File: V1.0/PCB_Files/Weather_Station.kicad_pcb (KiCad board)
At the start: 2 copper layers, 45 parts, among them J1 N091-2832TSWFG02-H14, J2 USB_B_Micro, J3 Conn_01x04_Pin, J4 Conn_01x04_Pin, J5 Conn_01x06_Pin, U1 STM32F103C8T6, U2 HDC1080DMBR, U3 AMS1117-3.3, U5 SRV05-4, Y1 X322516MLB4SI

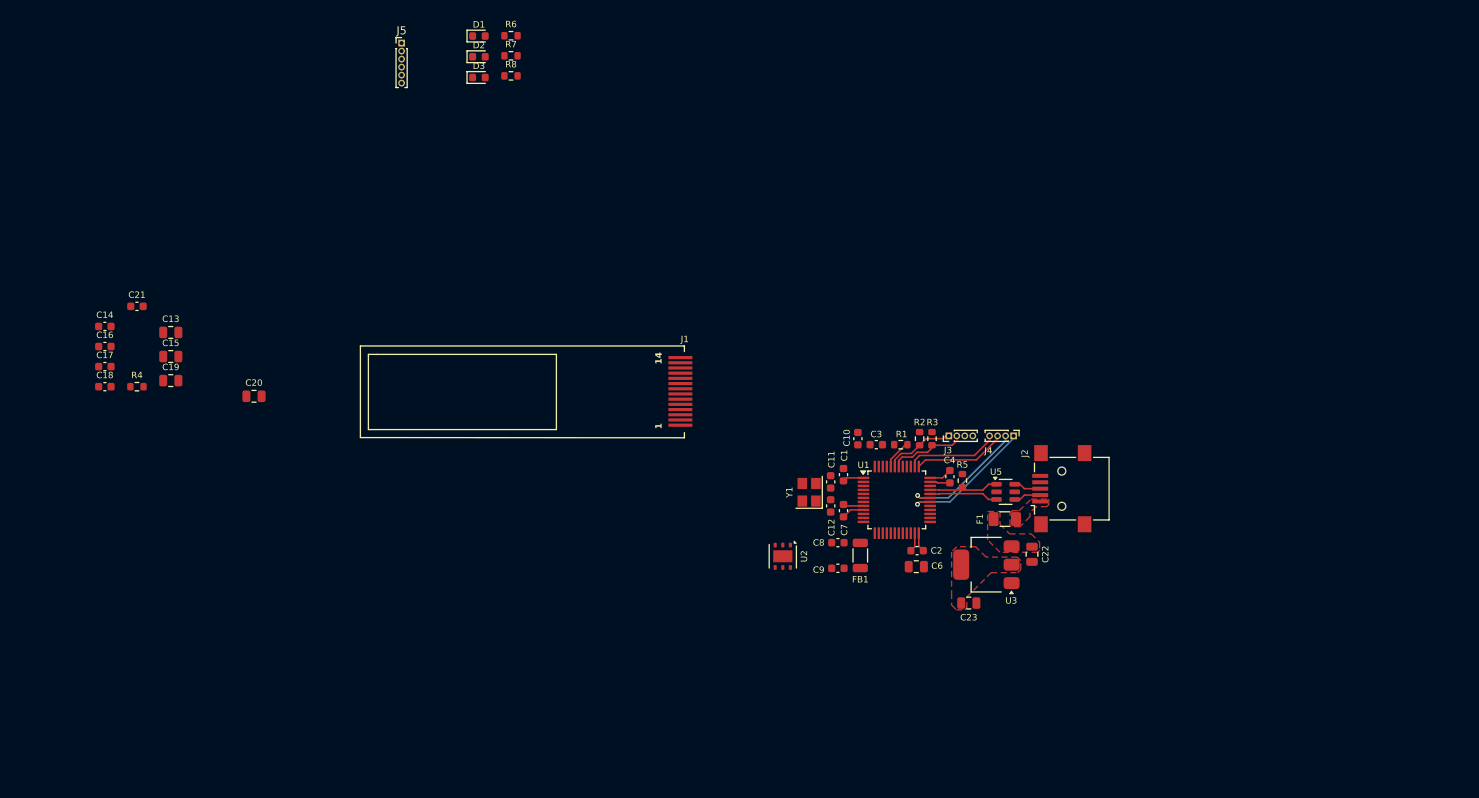
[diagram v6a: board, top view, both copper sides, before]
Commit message: Decided to not go with the display. Added Step file for display.
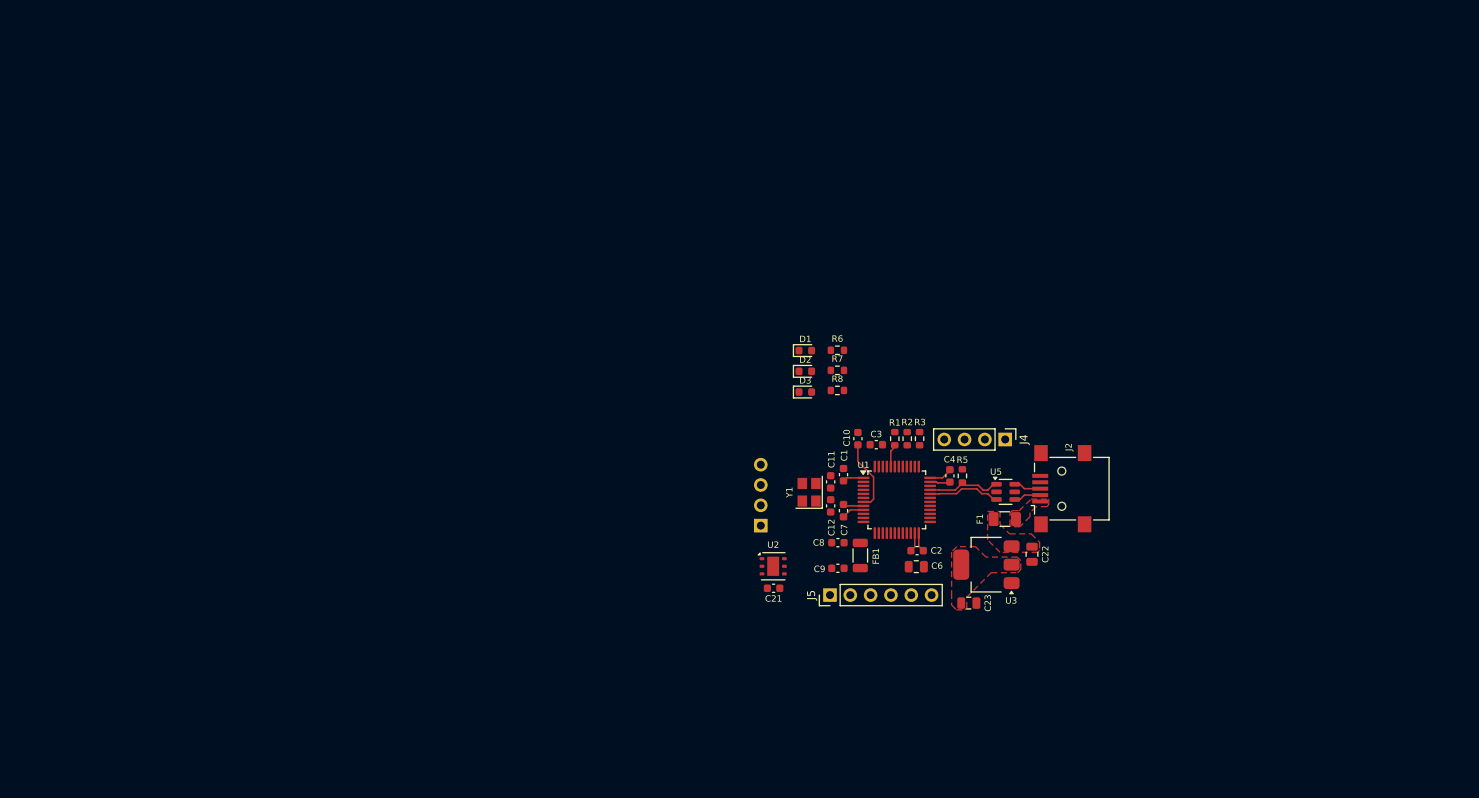
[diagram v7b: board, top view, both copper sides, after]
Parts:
- removed C13: 4u7/16V, Capacitor_SMD:C_0805_2012Metric
- removed C14: 100n/16V, Capacitor_SMD:C_0603_1608Metric
- removed C15: 2u2/16V, Capacitor_SMD:C_0805_2012Metric
- removed C16, C17: 1u/16V, Capacitor_SMD:C_0603_1608Metric
- removed C18: 100n/10V, Capacitor_SMD:C_0603_1608Metric
- removed C19, C20: 4u7/10V, Capacitor_SMD:C_0805_2012Metric
- removed R4: 910k, Resistor_SMD:R_0603_1608Metric
- J1: value N091-2832TSWFG02-H14 -> Conn_01x04_Socket; footprint Private_Connector_Display:OLED_SMD_128x32 -> Capacitor_SMD:C_0402_1005Metric; moved to B.Cu
- J3: footprint Connector_PinHeader_1.00mm:PinHeader_1x04_P1.00mm_Vertical -> Connector_PinHeader_2.54mm:PinHeader_1x04_P2.54mm_Vertical; moved to B.Cu
- J4: footprint Connector_PinHeader_1.00mm:PinHeader_1x04_P1.00mm_Vertical -> Connector_PinHeader_2.54mm:PinHeader_1x04_P2.54mm_Vertical
- J5: footprint Connector_PinHeader_1.00mm:PinHeader_1x06_P1.00mm_Vertical -> Connector_PinHeader_2.54mm:PinHeader_1x06_P2.54mm_Vertical
- moved J5 87.3 mm to (156.9, 94.8), turned to 90 degrees
- moved C21 87.0 mm to (149.9, 94.0)
- moved D3 56.7 mm to (153.9, 69.4)
- moved D1 56.7 mm to (153.9, 64.2)
- moved D2 56.7 mm to (153.9, 66.8)
- moved R6 56.7 mm to (157.9, 64.2)
- moved R8 56.7 mm to (157.9, 69.2)
- moved R7 56.7 mm to (157.9, 66.7)
- moved J3 26.0 mm to (148.3, 86.1), turned to 0 degrees
- moved J1 25.1 mm to (146.8, 88.7)
- moved U2 1.73 mm to (149.8, 91.2), turned to 0 degrees
- moved R2 1.55 mm to (166.6, 75.2)
- moved R3 1.55 mm to (168.2, 75.2)
- moved J4 1.14 mm to (178.8, 75.3)
- moved R1 1.06 mm to (165.1, 75.2), turned to -90 degrees
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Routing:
- net /USART1_TX: track 17.4 -> 0.00 mm, vias 1 -> 0
- net /USART1_RX: track 16.4 -> 0.00 mm, vias 1 -> 0
- net /SWDIO: track 11.7 -> 0.00 mm
- net /SWCLK: track 11.6 -> 0.00 mm
- net /I2C1_SCL: track 9.83 -> 0.00 mm
- net /NRST: track 0.00 -> 9.00 mm
- net /I2C1_SDA: track 8.83 -> 0.00 mm
- net /BOOT0: track 3.74 -> 2.87 mm

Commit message: Should be final component placement.
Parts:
- moved R6 10.2 mm to (153.0, 73.2)
- moved D1 9.80 mm to (149.9, 73.2)
- moved R7 9.49 mm to (153.0, 74.8)
- moved D2 8.94 mm to (149.9, 74.8)
- moved R8 8.72 mm to (153.0, 76.5)
- moved D3 8.08 mm to (149.9, 76.5)
- moved C23 3.45 mm to (173.2, 92.5)
- moved U3 3.45 mm to (175.4, 87.8)
- moved C22 3.45 mm to (181.1, 86.5)
- moved J2 2.85 mm to (186.0, 78.7)
- moved U5 2.81 mm to (179.4, 79.1)
- moved F1 2.59 mm to (179.3, 82.8)
- moved J5 1.29 mm to (155.8, 94.2)
- moved J4 0.90 mm to (178.8, 74.5)
- moved C21 0.50 mm to (149.4, 94.0)
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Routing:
- net /USB_D-: track 12.5 -> 7.33 mm
- net /USB_D+: track 12.5 -> 7.45 mm
- removed copper zone on F.Cu, net +3.3V
- removed copper zone on F.Cu, net /VBUS_IN
- removed copper zone on F.Cu, net VBUS
